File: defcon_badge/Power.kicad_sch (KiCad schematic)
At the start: 15 parts, among them J10 USB_C_Receptacle_USB2.0_16P, J11 JST-PH 2P, SW1 SS-12D00, U10 TP4056, U11 ME6211C33M5G

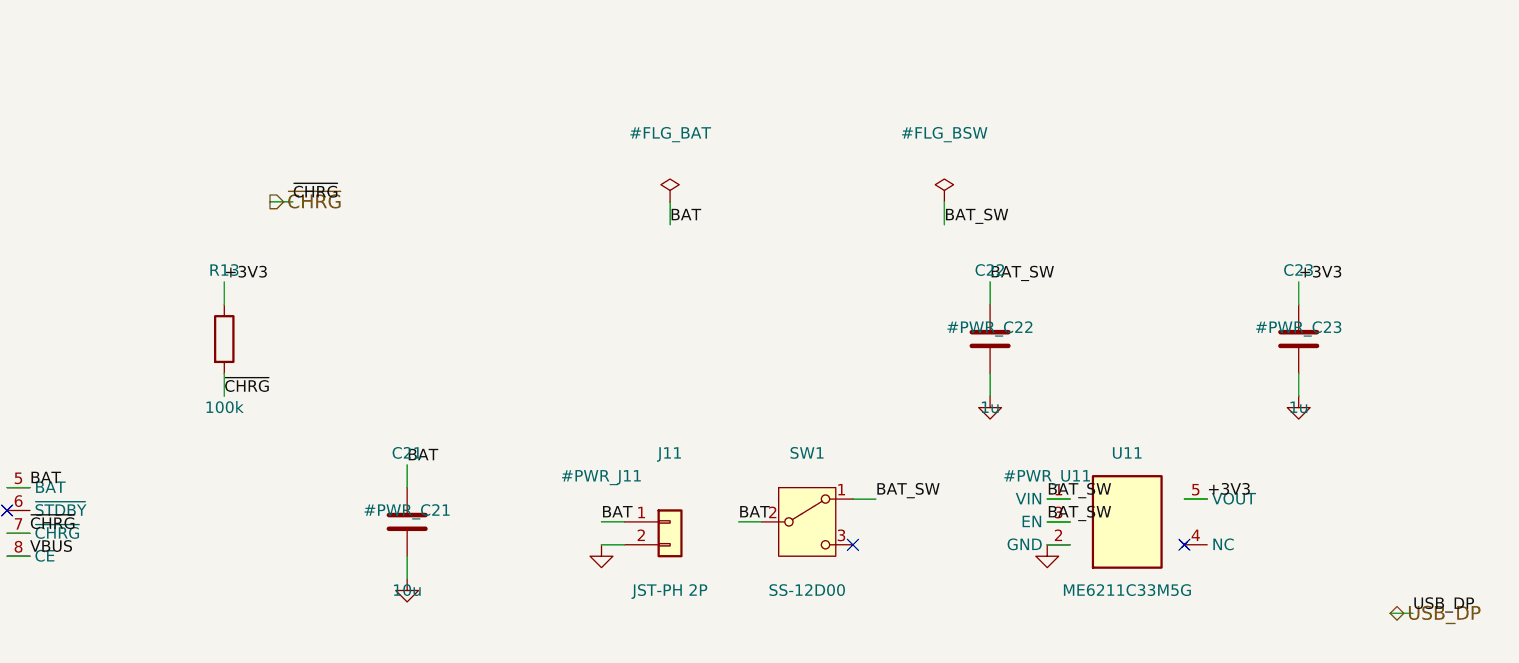
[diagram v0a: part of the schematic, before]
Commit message: Schematic: fix +3V3 power-tree (board was dead) + add review framework
The +3V3 rail was fragmented into 5 disconnected nets — child sheets emitted it
via sheet-local (label "+3V3") while MCU_Core used global power:+3V3 symbols, so
the LDO output reached zero loads and the whole board could not power up
(6 ERC errors incl. 5 power_pin_not_driven). Root-caused and fixed at the
GENERATOR level, then regenerated the sheets:

- kicad_sheet_gen.py: RAIL_NAMES + label_at_pin() routes rail nets through the
  global power: symbol (never a sheet-local label that can't cross hierarchy).
- gen_power_sheet.py: add #FLG_GND PWR_FLAG (GND was undriven); drop redundant
  #FLG_BAT (it shorted two power outputs -> pin_to_pin error).
- gen_io_sheet.py: restore SW23 (SYNC button) + BTN_SYNC — caught generator drift
  where the committed schematic had SW23 but the generator only made 3 buttons.

Result (authoritative kicad-cli ERC/netlist): ERC 6->0 errors, +3V3 unified
(5 nets -> 1), all power pins driven, no pin conflicts. 4/5 gates pass (the 5th
is the 7 intentional RP2040 GPIO spares).

Adds schematic_phase/ — an authoritative, repeatable schematic-review framework
mirroring placement_phase_2/ (HARNESS, LEDGER, metrics.jsonl, and tools/sch_health.py
which derives all metrics from kicad-cli, not the analyzer that over-merges nets).

Co-Authored-By: Claude Opus 4.8 (1M context) <noreply@anthropic.com>
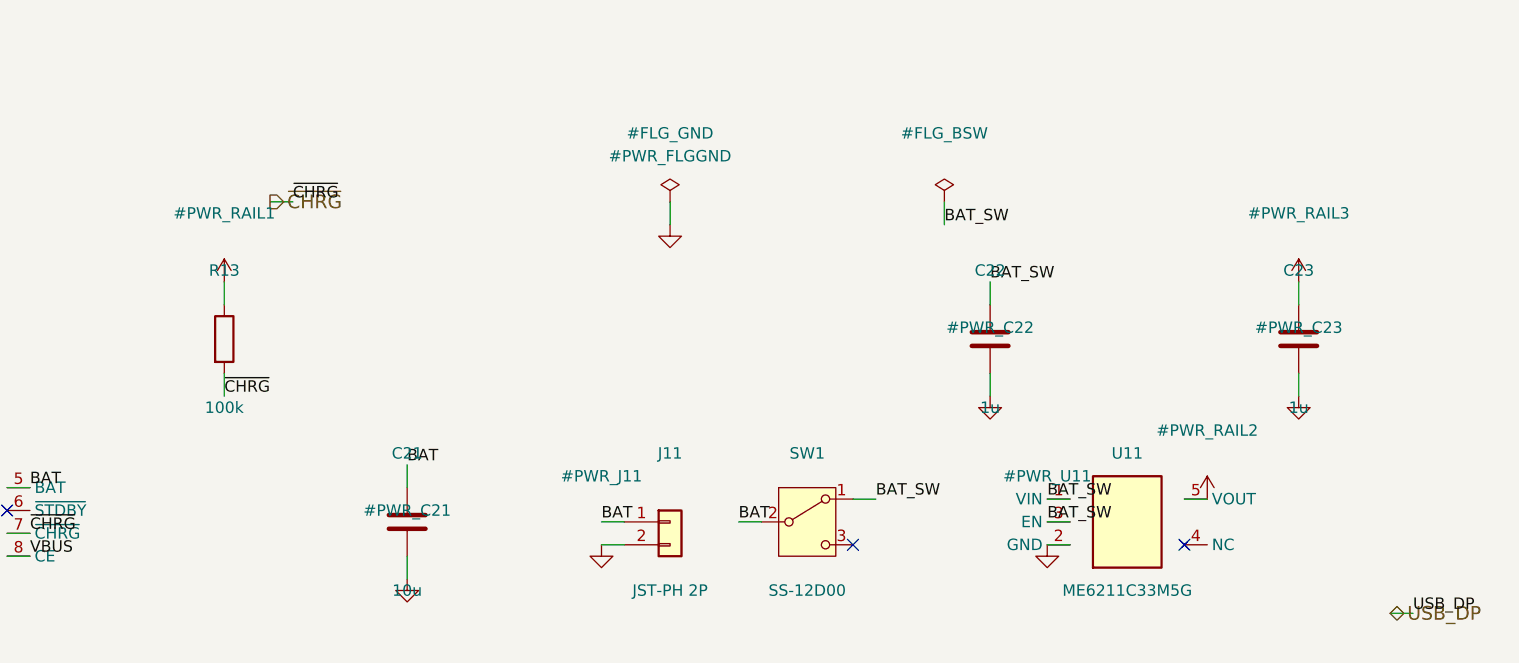
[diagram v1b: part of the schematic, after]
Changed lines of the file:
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@@
+	)
+	(symbol
+		(lib_id "power:+3V3")
+		(at 160.02 63.50 0)
+		(unit 1)
+		(body_style 1)
+		(exclude_from_sim no)
+		(in_bom yes)
+		(on_board yes)
+		(in_pos_files yes)
+		(dnp no)
+		(fields_autoplaced yes)
+		(property "Reference" "#PWR_RAIL1" (at 160.02 55.88 0) (effects (font (size 1.27 1.27))))
+		(property "Value" "+3V3" (at 160.02 71.12 0) (effects (font (size 1.27 1.27)) (hide yes)))
+		(property "Footprint" "" (at 160.02 63.50 0) (show_name no) (hide yes) (effects (font (size 1.27 1.27))))
+		(property "Datasheet" "" (at 160.02 63.50 0) (show_name no) (hide yes) (effects (font (size 1.27 1.27))))
+		(property "Description" "" (at 160.02 63.50 0) (show_name no) (hide yes) (effects (font (size 1.27 1.27))))
+		(pin "1")
+		(instances
+			(project "defcon_badge"
+				(path "/8c0b3d8b-46d3-4173-ab1e-a61765f77d61/5744f316-b81d-4687-a6bb-e0b6cbd3f68c"
+					(reference "#PWR_RAIL1")
+					(unit 1)
+				)
+			)
+		)
 	)
 	(symbol
@@
 	)
 	(symbol
+		(lib_id "power:+3V3")
+		(at 269.24 87.63 0)
+		(unit 1)
+		(body_style 1)
+		(exclude_from_sim no)
+		(in_bom yes)
+		(on_board yes)
+		(in_pos_files yes)
+		(dnp no)
+		(fields_autoplaced yes)
+		(property "Reference" "#PWR_RAIL2" (at 269.24 80.01 0) (effects (font (size 1.27 1.27))))
+		(property "Value" "+3V3" (at 269.24 95.25 0) (effects (font (size 1.27 1.27)) (hide yes)))
+		(property "Footprint" "" (at 269.24 87.63 0) (show_name no) (hide yes) (effects (font (size 1.27 1.27))))
+		(property "Datasheet" "" (at 269.24 87.63 0) (show_name no) (hide yes) (effects (font (size 1.27 1.27))))
+		(property "Description" "" (at 269.24 87.63 0) (show_name no) (hide yes) (effects (font (size 1.27 1.27))))
+		(pin "1")
+		(instances
+			(project "defcon_badge"
+				(path "/8c0b3d8b-46d3-4173-ab1e-a61765f77d61/5744f316-b81d-4687-a6bb-e0b6cbd3f68c"
+					(reference "#PWR_RAIL2")
+					(unit 1)
+				)
+			)
+		)
+	)
+	(symbol
+		(lib_id "power:+3V3")
+		(at 279.40 63.50 0)
+		(unit 1)
+		(body_style 1)
+		(exclude_from_sim no)
+		(in_bom yes)
+		(on_board yes)
+		(in_pos_files yes)
+		(dnp no)
+		(fields_autoplaced yes)
+		(property "Reference" "#PWR_RAIL3" (at 279.40 55.88 0) (effects (font (size 1.27 1.27))))
+		(property "Value" "+3V3" (at 279.40 71.12 0) (effects (font (size 1.27 1.27)) (hide yes)))
+		(property "Footprint" "" (at 279.40 63.50 0) (show_name no) (hide yes) (effects (font (size 1.27 1.27))))
+		(property "Datasheet" "" (at 279.40 63.50 0) (show_name no) (hide yes) (effects (font (size 1.27 1.27))))
+		(property "Description" "" (at 279.40 63.50 0) (show_name no) (hide yes) (effects (font (size 1.27 1.27))))
+		(pin "1")
+		(instances
+			(project "defcon_badge"
+				(path "/8c0b3d8b-46d3-4173-ab1e-a61765f77d61/5744f316-b81d-4687-a6bb-e0b6cbd3f68c"
+					(reference "#PWR_RAIL3")
+					(unit 1)
+				)
+			)
+		)
+	)
+	(symbol
 		(lib_id "power:GND")
 		(at 279.40 76.20 0)
@@
 		(dnp no)
 		(fields_autoplaced yes)
-		(property "Reference" "#FLG_BAT" (at 209.55 46.99 0) (effects (font (size 1.27 1.27))))
+		(property "Reference" "#FLG_GND" (at 209.55 46.99 0) (effects (font (size 1.27 1.27))))
 		(property "Value" "PWR_FLAG" (at 209.55 62.23 0) (effects (font (size 1.27 1.27)) (hide yes)))
 		(property "Footprint" "" (at 209.55 54.61 0) (show_name no) (hide yes) (effects (font (size 1.27 1.27))))
 		(property "Datasheet" "" (at 209.55 54.61 0) (show_name no) (hide yes) (effects (font (size 1.27 1.27))))
-		(property "Description" "Declare BAT externally driven" (at 209.55 54.61 0) (show_name no) (hide yes) (effects (font (size 1.27 1.27))))
-		(pin "1")
-		(instances
-			(project "defcon_badge"
-				(path "/8c0b3d8b-46d3-4173-ab1e-a61765f77d61/5744f316-b81d-4687-a6bb-e0b6cbd3f68c"
-					(reference "#FLG_BAT")
+		(property "Description" "Declare GND as a power source (sinks-only net)" (at 209.55 54.61 0) (show_name no) (hide yes) (effects (font (size 1.27 1.27))))
+		(pin "1")
+		(instances
+			(project "defcon_badge"
+				(path "/8c0b3d8b-46d3-4173-ab1e-a61765f77d61/5744f316-b81d-4687-a6bb-e0b6cbd3f68c"
+					(reference "#FLG_GND")
+					(unit 1)
+				)
+			)
+		)
+	)
+	(symbol
+		(lib_id "power:GND")
+		(at 209.55 57.15 0)
+		(unit 1)
+		(body_style 1)
+		(exclude_from_sim no)
+		(in_bom yes)
+		(on_board yes)
+		(in_pos_files yes)
+		(dnp no)
+		(fields_autoplaced yes)
+		(property "Reference" "#PWR_FLGGND" (at 209.55 49.53 0) (effects (font (size 1.27 1.27))))
+		(property "Value" "GND" (at 209.55 64.77 0) (effects (font (size 1.27 1.27)) (hide yes)))
+		(property "Footprint" "" (at 209.55 57.15 0) (show_name no) (hide yes) (effects (font (size 1.27 1.27))))
+		(property "Datasheet" "" (at 209.55 57.15 0) (show_name no) (hide yes) (effects (font (size 1.27 1.27))))
+		(property "Description" "" (at 209.55 57.15 0) (show_name no) (hide yes) (effects (font (size 1.27 1.27))))
+		(pin "1")
+		(instances
+			(project "defcon_badge"
+				(path "/8c0b3d8b-46d3-4173-ab1e-a61765f77d61/5744f316-b81d-4687-a6bb-e0b6cbd3f68c"
+					(reference "#PWR_FLGGND")
 					(unit 1)
 				)
@@
 	(label "VBUS" (at 138.43 93.98 0) (effects (font (size 1.27 1.27)) (justify left bottom)))
 	(label "PROG_SET" (at 115.57 123.19 0) (effects (font (size 1.27 1.27)) (justify left bottom)))
-	(label "+3V3" (at 160.02 63.50 0) (effects (font (size 1.27 1.27)) (justify left bottom)))
 	(label "~{CHRG}" (at 160.02 76.20 0) (effects (font (size 1.27 1.27)) (justify left bottom)))
 	(label "BAT" (at 180.34 83.82 0) (effects (font (size 1.27 1.27)) (justify left bottom)))
@@
 	(label "BAT_SW" (at 251.46 87.63 0) (effects (font (size 1.27 1.27)) (justify left bottom)))
 	(label "BAT_SW" (at 251.46 90.17 0) (effects (font (size 1.27 1.27)) (justify left bottom)))
-	(label "+3V3" (at 269.24 87.63 0) (effects (font (size 1.27 1.27)) (justify left bottom)))
-	(label "+3V3" (at 279.40 63.50 0) (effects (font (size 1.27 1.27)) (justify left bottom)))
 	(label "BAT" (at 154.94 148.59 0) (effects (font (size 1.27 1.27)) (justify left bottom)))
 	(label "VBAT_SENSE" (at 154.94 161.29 0) (effects (font (size 1.27 1.27)) (justify left bottom)))
 	(label "VBAT_SENSE" (at 154.94 168.91 0) (effects (font (size 1.27 1.27)) (justify left bottom)))
 	(label "VBUS" (at 74.93 62.23 0) (effects (font (size 1.27 1.27)) (justify left bottom)))
-	(label "BAT" (at 209.55 57.15 0) (effects (font (size 1.27 1.27)) (justify left bottom)))
 	(label "BAT_SW" (at 240.03 57.15 0) (effects (font (size 1.27 1.27)) (justify left bottom)))
 	(label "USB_DP" (at 292.10 100.33 0) (effects (font (size 1.27 1.27)) (justify left bottom)))
